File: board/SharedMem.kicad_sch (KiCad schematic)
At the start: 10 parts, among them U19 HM628512LP-5, U20 HM628512LP-5, U21 HM628512LP-5, U22 HM628512LP-5, U23 74F139

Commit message: Board V1.1G
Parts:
- U19, U20, U21, U22: footprint Package_DIP:DIP-32_W15.24mm_Socket_LongPads -> Package_SO:SOP-32_11.305x20.495mm_P1.27mm
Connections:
- net A0 renamed A_MEM0
- net A1 renamed A_MEM1
- net A10 renamed A_MEM10
- net A11 renamed A_MEM11
- net A12 renamed A_MEM12
- net A2 renamed A_MEM2
- net A3 renamed A_MEM3
- net A4 renamed A_MEM4
- net A5 renamed A_MEM5
- net A6 renamed A_MEM6
- net A7 renamed A_MEM7
- net A8 renamed A_MEM8
- net A9 renamed A_MEM9
- net D0 renamed D_MEM0
- net D1 renamed D_MEM1
- net D2 renamed D_MEM2
- net D3 renamed D_MEM3
- net D4 renamed D_MEM4
- net D5 renamed D_MEM5
- net D6 renamed D_MEM6
- net D7 renamed D_MEM7

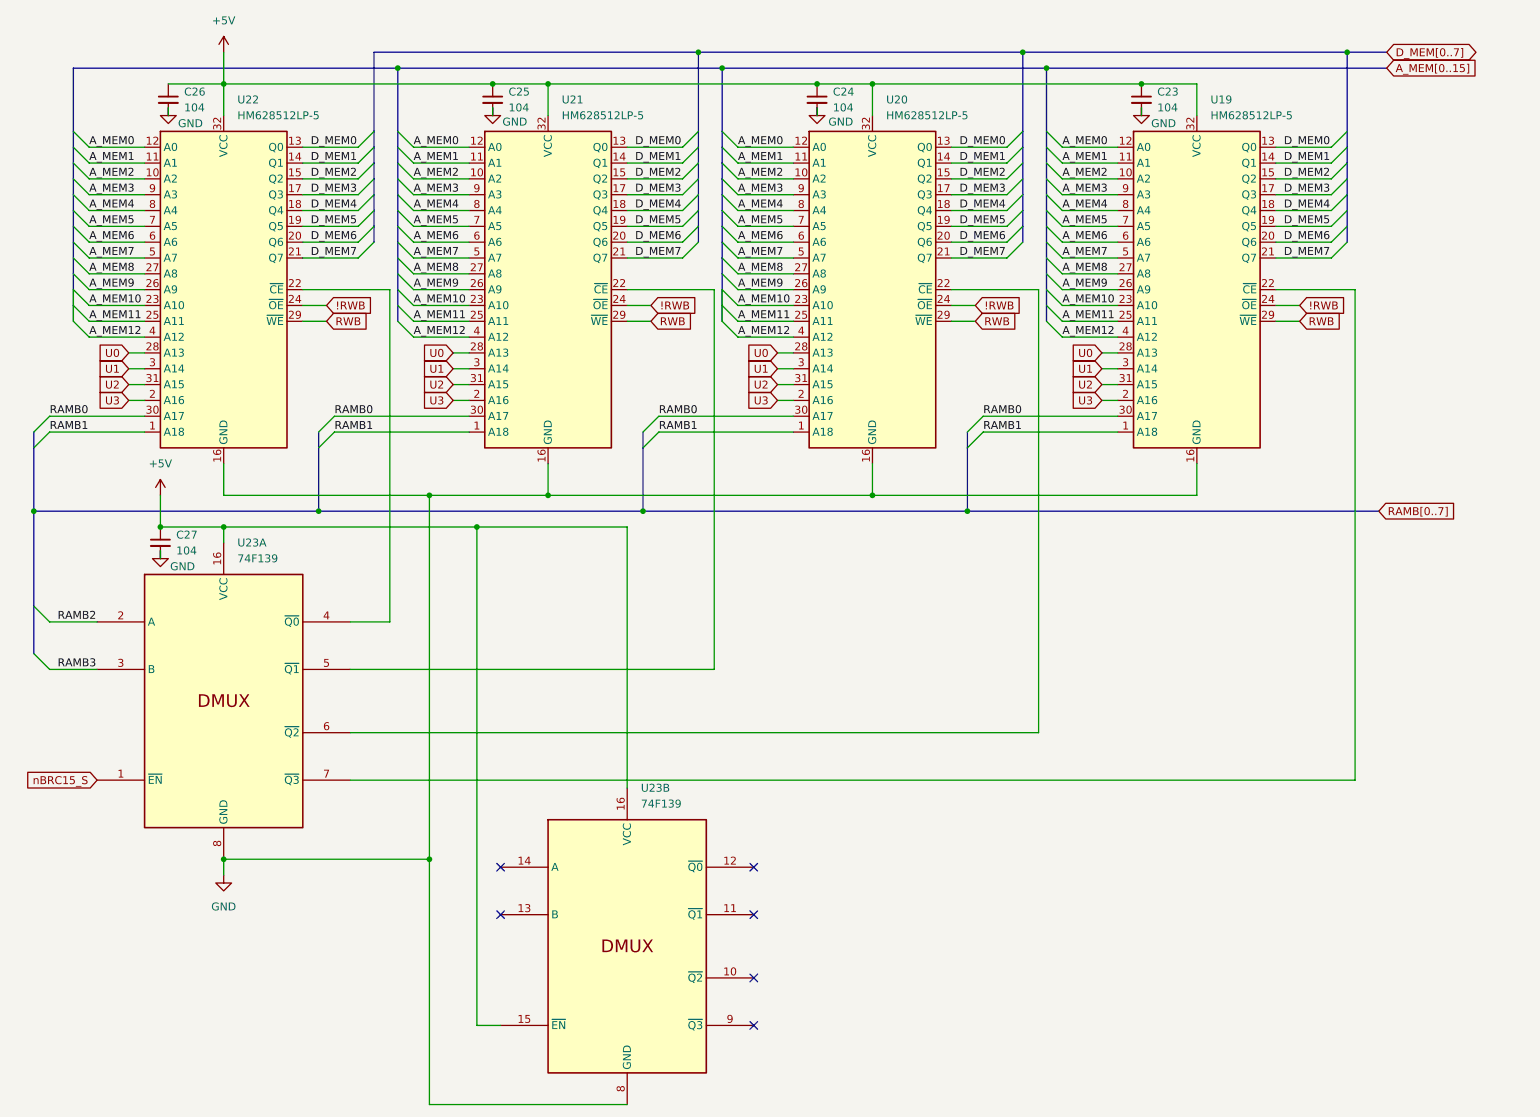
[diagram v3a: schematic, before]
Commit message: V1.3C without board traces
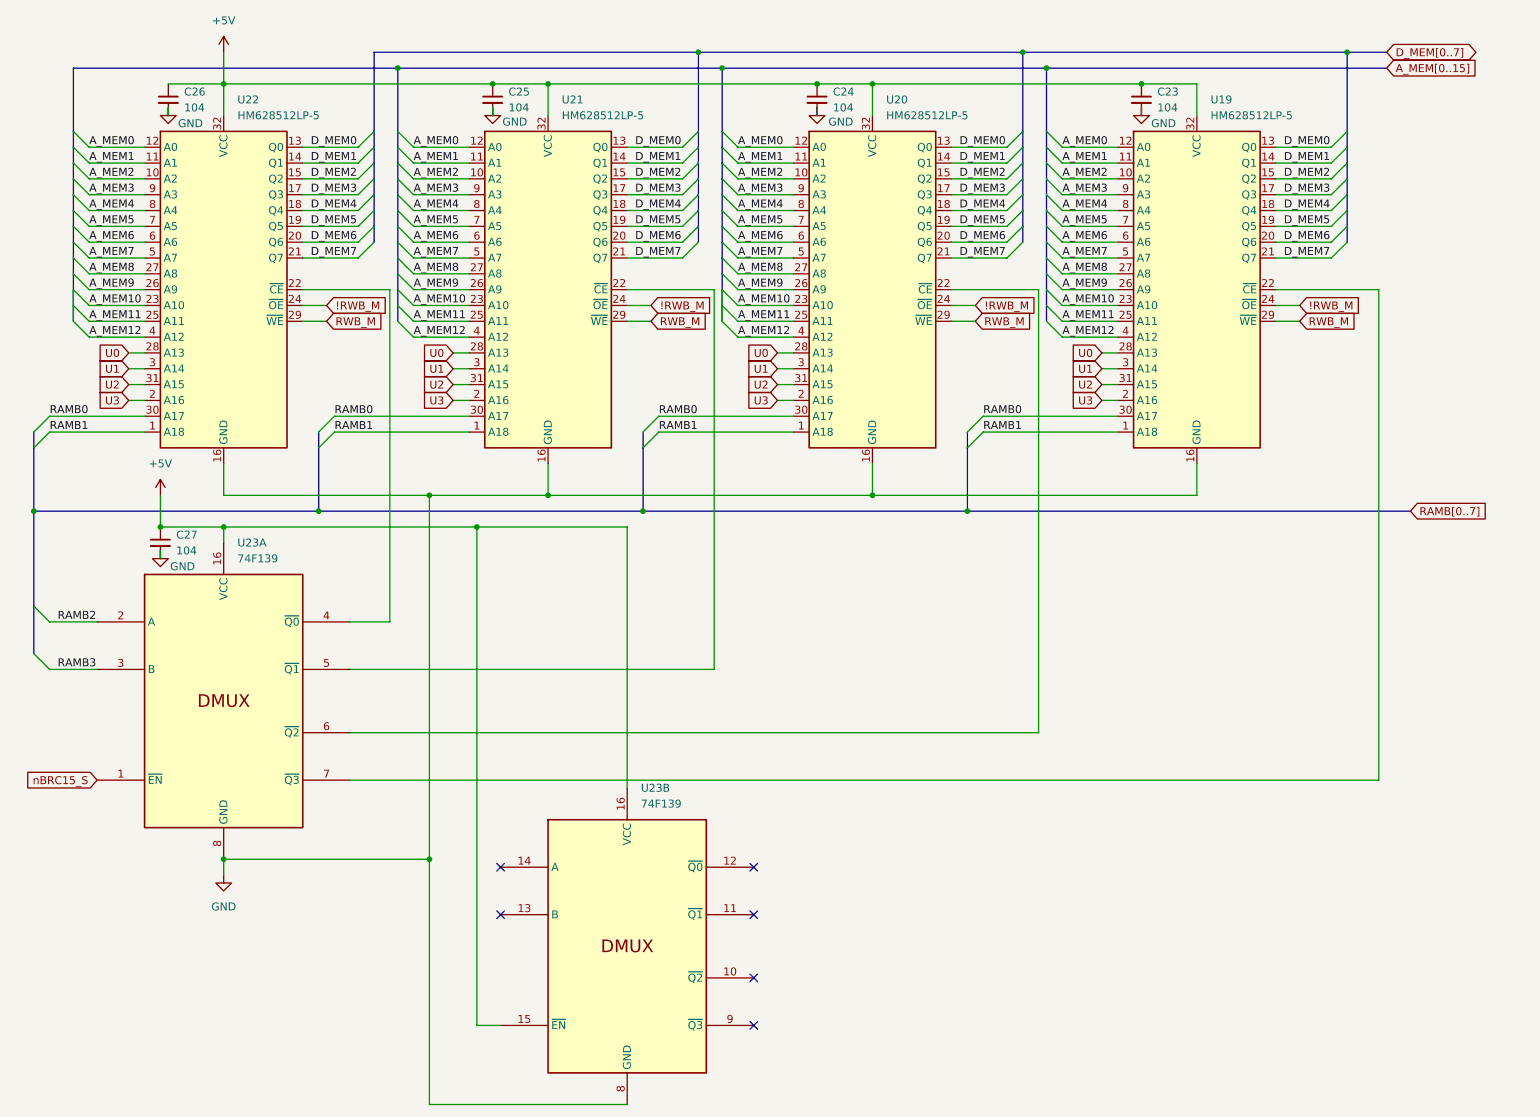
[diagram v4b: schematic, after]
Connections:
- net !RWB renamed !RWB_M
- net RWB renamed RWB_M
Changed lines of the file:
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@@
 	(title_block
 		(title "Shared RAM Banks")
-		(date "2025-04-15")
-		(rev "1.3")
+		(date "2025-04-23")
+		(rev "1.3C")
 		(company "Data Tuning")
 		(comment 1 "Hydra 16")
@@
 	(wire
 		(pts
-			(xy 232.41 148.59) (xy 232.41 69.85)
+			(xy 236.22 148.59) (xy 236.22 69.85)
 		)
 		(stroke
@@
 	(wire
 		(pts
-			(xy 71.12 148.59) (xy 232.41 148.59)
+			(xy 71.12 148.59) (xy 236.22 148.59)
 		)
 		(stroke
@@
 	(wire
 		(pts
-			(xy 219.71 69.85) (xy 232.41 69.85)
+			(xy 219.71 69.85) (xy 236.22 69.85)
 		)
 		(stroke
@@
 	(bus
 		(pts
-			(xy 170.18 105.41) (xy 236.22 105.41)
+			(xy 170.18 105.41) (xy 241.3 105.41)
 		)
 		(stroke
@@
 	(global_label "RAMB[0..7]"
 		(shape input)
-		(at 236.22 105.41 0)
+		(at 241.3 105.41 0)
 		(fields_autoplaced yes)
 		(effects
@@
 		)
 		(property "Intersheetrefs" "${INTERSHEET_REFS}"
-			(at 249.6072 105.41 0)
+			(at 254.6872 105.41 0)
 			(effects
 				(font
@@
 		)
 	)
-	(global_label "RWB"
+	(global_label "RWB_M"
 		(shape input)
 		(at 119.38 74.93 0)
@@
 		)
 		(property "Intersheetrefs" "${INTERSHEET_REFS}"
-			(at 112.4034 74.93 0)
+			(at 128.7756 74.93 0)
 			(effects
 				(font
 					(size 1.27 1.27)
 				)
-				(justify right)
+				(justify left)
 				(hide yes)
 			)
@@
 		)
 	)
-	(global_label "!RWB"
+	(global_label "!RWB_M"
 		(shape input)
 		(at 119.38 72.39 0)
@@
 		)
 		(property "Intersheetrefs" "${INTERSHEET_REFS}"
-			(at 126.9614 72.39 0)
+			(at 129.3804 72.39 0)
 			(effects
 				(font
@@
 		)
 	)
-	(global_label "!RWB"
+	(global_label "!RWB_M"
 		(shape input)
 		(at 223.52 72.39 0)
@@
 		)
 		(property "Intersheetrefs" "${INTERSHEET_REFS}"
-			(at 231.1014 72.39 0)
+			(at 233.5204 72.39 0)
 			(effects
 				(font
@@
 		)
 	)
-	(global_label "RWB"
+	(global_label "RWB_M"
 		(shape input)
 		(at 171.45 74.93 0)
@@
 		)
 		(property "Intersheetrefs" "${INTERSHEET_REFS}"
-			(at 164.4734 74.93 0)
+			(at 180.8456 74.93 0)
 			(effects
 				(font
 					(size 1.27 1.27)
 				)
-				(justify right)
+				(justify left)
 				(hide yes)
 			)
@@
 		)
 	)
-	(global_label "!RWB"
+	(global_label "!RWB_M"
 		(shape input)
 		(at 171.45 72.39 0)
@@
 		)
 		(property "Intersheetrefs" "${INTERSHEET_REFS}"
-			(at 179.0314 72.39 0)
+			(at 181.4504 72.39 0)
 			(effects
 				(font
@@
 		)
 	)
-	(global_label "!RWB"
+	(global_label "!RWB_M"
 		(shape input)
 		(at 67.31 72.39 0)
@@
 		)
 		(property "Intersheetrefs" "${INTERSHEET_REFS}"
-			(at 74.8914 72.39 0)
+			(at 77.3104 72.39 0)
 			(effects
 				(font
@@
 		)
 	)
-	(global_label "RWB"
+	(global_label "RWB_M"
 		(shape input)
 		(at 67.31 74.93 0)
@@
 		)
 		(property "Intersheetrefs" "${INTERSHEET_REFS}"
-			(at 60.3334 74.93 0)
+			(at 76.7056 74.93 0)
 			(effects
 				(font
 					(size 1.27 1.27)
 				)
-				(justify right)
+				(justify left)
 				(hide yes)
 			)
 		)
 	)
-	(global_label "RWB"
+	(global_label "RWB_M"
 		(shape input)
 		(at 223.52 74.93 0)
@@
 		)
 		(property "Intersheetrefs" "${INTERSHEET_REFS}"
-			(at 216.5434 74.93 0)
+			(at 232.9156 74.93 0)
 			(effects
 				(font
 					(size 1.27 1.27)
 				)
-				(justify right)
+				(justify left)
 				(hide yes)
 			)

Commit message: V1.4E
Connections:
- net A_MEM0 renamed A0
- net A_MEM1 renamed A1
- net A_MEM10 renamed A10
- net A_MEM11 renamed A11
- net A_MEM12 renamed A12
- net A_MEM2 renamed A2
- net A_MEM3 renamed A3
- net A_MEM4 renamed A4
- net A_MEM5 renamed A5
- net A_MEM6 renamed A6
- net A_MEM7 renamed A7
- net A_MEM8 renamed A8
- net A_MEM9 renamed A9
- net D_MEM0 renamed D0
- net D_MEM1 renamed D1
- net D_MEM2 renamed D2
- net D_MEM3 renamed D3
- net D_MEM4 renamed D4
- net D_MEM5 renamed D5
- net D_MEM6 renamed D6
- net D_MEM7 renamed D7

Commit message: Version 1.7A: More rearrangement, partial wiring of PDB, addition of W register
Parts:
- renumbered C27 to C33, C26 to C34, C25 to C35, C24 to C36, C23 to C37, U22 to U25, U23 to U26, U21 to U27, U20 to U28, U19 to U29
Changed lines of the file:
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@@
 	(title_block
 		(title "Shared RAM Banks")
-		(date "2025-04-23")
-		(rev "1.3C")
+		(date "2025-09-18")
+		(rev "1.6F")
 		(company "Data Tuning")
 		(comment 1 "Hydra 16")
@@
 		(dnp no)
 		(fields_autoplaced yes)
-		(property "Reference" "U20"
+		(property "Reference" "U28"
 			(at 157.1341 39.37 0)
 			(effects
@@
 			(project "hydra-16"
 				(path "/ef29fc71-3fec-48b5-8a1a-46bee537a98c/0b66303c-ed46-41df-a285-d041c923c3ce"
-					(reference "U20")
+					(reference "U28")
 					(unit 1)
 				)
@@
 		(dnp no)
 		(fields_autoplaced yes)
-		(property "Reference" "C26"
+		(property "Reference" "C34"
 			(at 44.45 38.1062 0)
 			(effects
@@
 			(project "6502_x256"
 				(path "/ef29fc71-3fec-48b5-8a1a-46bee537a98c/0b66303c-ed46-41df-a285-d041c923c3ce"
-					(reference "C26")
+					(reference "C34")
 					(unit 1)
 				)
@@
 		(dnp no)
 		(fields_autoplaced yes)
-		(property "Reference" "C24"
+		(property "Reference" "C36"
 			(at 148.59 38.1062 0)
 			(effects
@@
 			(project "6502_x256"
 				(path "/ef29fc71-3fec-48b5-8a1a-46bee537a98c/0b66303c-ed46-41df-a285-d041c923c3ce"
-					(reference "C24")
+					(reference "C36")
 					(unit 1)
 				)
@@
 		(on_board yes)
 		(dnp no)
-		(property "Reference" "#PWR028"
+		(property "Reference" "#PWR017"
 			(at 93.98 46.99 0)
 			(effects
@@
 			(project "6502_x256"
 				(path "/ef29fc71-3fec-48b5-8a1a-46bee537a98c/0b66303c-ed46-41df-a285-d041c923c3ce"
-					(reference "#PWR028")
+					(reference "#PWR017")
 					(unit 1)
 				)
@@
 		(dnp no)
 		(fields_autoplaced yes)
-		(property "Reference" "#PWR041"
+		(property "Reference" "#PWR012"
 			(at 40.64 106.68 0)
 			(effects
@@
 			(project "hydra-16"
 				(path "/ef29fc71-3fec-48b5-8a1a-46bee537a98c/0b66303c-ed46-41df-a285-d041c923c3ce"
-					(reference "#PWR041")
+					(reference "#PWR012")
 					(unit 1)
 				)
@@
 		(on_board yes)
 		(dnp no)
-		(property "Reference" "#PWR029"
+		(property "Reference" "#PWR014"
 			(at 41.91 46.99 0)
 			(effects
@@
 			(project "6502_x256"
 				(path "/ef29fc71-3fec-48b5-8a1a-46bee537a98c/0b66303c-ed46-41df-a285-d041c923c3ce"
-					(reference "#PWR029")
+					(reference "#PWR014")
 					(unit 1)
 				)
@@
 		(dnp no)
 		(fields_autoplaced yes)
-		(property "Reference" "C27"
+		(property "Reference" "C33"
 			(at 43.18 109.2262 0)
 			(effects
@@
 			(project "6502_x256"
 				(path "/ef29fc71-3fec-48b5-8a1a-46bee537a98c/0b66303c-ed46-41df-a285-d041c923c3ce"
-					(reference "C27")
+					(reference "C33")
 					(unit 1)
 				)
@@
 		(dnp no)
 		(fields_autoplaced yes)
-		(property "Reference" "U19"
+		(property "Reference" "U29"
 			(at 209.2041 39.37 0)
 			(effects
@@
 			(project "hydra-16"
 				(path "/ef29fc71-3fec-48b5-8a1a-46bee537a98c/0b66303c-ed46-41df-a285-d041c923c3ce"
-					(reference "U19")
+					(reference "U29")
 					(unit 1)
 				)
@@
 		(on_board yes)
 		(dnp no)
-		(property "Reference" "#PWR026"
+		(property "Reference" "#PWR019"
 			(at 198.12 46.99 0)
 			(effects
@@
 			(project "6502_x256"
 				(path "/ef29fc71-3fec-48b5-8a1a-46bee537a98c/0b66303c-ed46-41df-a285-d041c923c3ce"
-					(reference "#PWR026")
+					(reference "#PWR019")
 					(unit 1)
 				)
@@
 		(dnp no)
 		(fields_autoplaced yes)
-		(property "Reference" "C25"
+		(property "Reference" "C35"
 			(at 96.52 38.1062 0)
 			(effects
@@
 			(project "6502_x256"
 				(path "/ef29fc71-3fec-48b5-8a1a-46bee537a98c/0b66303c-ed46-41df-a285-d041c923c3ce"
-					(reference "C25")
+					(reference "C35")
 					(unit 1)
 				)
@@
 		(dnp no)
 		(fields_autoplaced yes)
-		(property "Reference" "U23"
+		(property "Reference" "U26"
 			(at 117.7641 149.86 0)
 			(effects
@@
 			(project "hydra-16"
 				(path "/ef29fc71-3fec-48b5-8a1a-46bee537a98c/0b66303c-ed46-41df-a285-d041c923c3ce"
-					(reference "U23")
+					(reference "U26")
 					(unit 2)
 				)
@@
 		(on_board yes)
 		(dnp no)
-		(property "Reference" "#PWR027"
+		(property "Reference" "#PWR018"
 			(at 146.05 46.99 0)
 			(effects
@@
 			(project "6502_x256"
 				(path "/ef29fc71-3fec-48b5-8a1a-46bee537a98c/0b66303c-ed46-41df-a285-d041c923c3ce"
-					(reference "#PWR027")
+					(reference "#PWR018")
 					(unit 1)
 				)
@@
 		(dnp no)
 		(fields_autoplaced yes)
-		(property "Reference" "U22"
+		(property "Reference" "U25"
 			(at 52.9941 39.37 0)
 			(effects
@@
 			(project "hydra-16"
 				(path "/ef29fc71-3fec-48b5-8a1a-46bee537a98c/0b66303c-ed46-41df-a285-d041c923c3ce"
-					(reference "U22")
+					(reference "U25")
 					(unit 1)
 				)
@@
 		(dnp no)
 		(fields_autoplaced yes)
-		(property "Reference" "C23"
+		(property "Reference" "C37"
 			(at 200.66 38.1062 0)
 			(effects
@@
 			(project "6502_x256"
 				(path "/ef29fc71-3fec-48b5-8a1a-46bee537a98c/0b66303c-ed46-41df-a285-d041c923c3ce"
-					(reference "C23")
+					(reference "C37")
 					(unit 1)
 				)
@@
 		(dnp no)
 		(fields_autoplaced yes)
-		(property "Reference" "#PWR06"
+		(property "Reference" "#PWR016"
 			(at 50.8 170.18 0)
 			(effects
@@
 			(project ""
 				(path "/ef29fc71-3fec-48b5-8a1a-46bee537a98c/0b66303c-ed46-41df-a285-d041c923c3ce"
-					(reference "#PWR06")
+					(reference "#PWR016")
 					(unit 1)
 				)
@@
 		(dnp no)
 		(fields_autoplaced yes)
-		(property "Reference" "#PWR05"
+		(property "Reference" "#PWR015"
 			(at 50.8 35.56 0)
 			(effects
@@
 			(project ""
 				(path "/ef29fc71-3fec-48b5-8a1a-46bee537a98c/0b66303c-ed46-41df-a285-d041c923c3ce"
-					(reference "#PWR05")
+					(reference "#PWR015")
 					(unit 1)
 				)
@@
 		(dnp no)
 		(fields_autoplaced yes)
-		(property "Reference" "U21"
+		(property "Reference" "U27"
 			(at 105.0641 39.37 0)
 			(effects
@@
 			(project "6502_x256"
 				(path "/ef29fc71-3fec-48b5-8a1a-46bee537a98c/0b66303c-ed46-41df-a285-d041c923c3ce"
-					(reference "U21")
+					(reference "U27")
 					(unit 1)
 				)
@@
 		(dnp no)
 		(fields_autoplaced yes)
-		(property "Reference" "U23"
+		(property "Reference" "U26"
 			(at 52.9941 110.49 0)
 			(effects
@@
 			(project ""
 				(path "/ef29fc71-3fec-48b5-8a1a-46bee537a98c/0b66303c-ed46-41df-a285-d041c923c3ce"
-					(reference "U23")
+					(reference "U26")
 					(unit 1)
 				)
@@
 		(on_board yes)
 		(dnp no)
-		(property "Reference" "#PWR030"
+		(property "Reference" "#PWR013"
 			(at 40.64 118.11 0)
 			(effects
@@
 			(project "6502_x256"
 				(path "/ef29fc71-3fec-48b5-8a1a-46bee537a98c/0b66303c-ed46-41df-a285-d041c923c3ce"
-					(reference "#PWR030")
+					(reference "#PWR013")
 					(unit 1)
 				)

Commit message: Version 1.7A: Partial wireup
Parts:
- removed unit 2 of U26
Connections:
- no-connect marks 6 -> 0
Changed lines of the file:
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@@
 		(title "Shared RAM Banks")
 		(date "2025-09-18")
-		(rev "1.6F")
+		(rev "1.7A")
 		(company "Data Tuning")
 		(comment 1 "Hydra 16")
@@
 	)
 	(junction
-		(at 91.44 107.95)
-		(diameter 0)
-		(color 0 0 0 0)
-	)
-	(junction
 		(at 130.81 34.29)
 		(diameter 0)
@@
 	)
 	(junction
-		(at 83.82 161.29)
-		(diameter 0)
-		(color 0 0 0 0)
-	)
-	(junction
 		(at 146.05 36.83)
 		(diameter 0)
@@
 		(color 0 0 0 0)
 	)
-	(no_connect
-		(at 135.89 162.56)
-	)
-	(no_connect
-		(at 135.89 180.34)
-	)
-	(no_connect
-		(at 135.89 187.96)
-	)
-	(no_connect
-		(at 95.25 170.18)
-	)
-	(no_connect
-		(at 95.25 162.56)
-	)
-	(no_connect
-		(at 135.89 170.18)
-	)
 	(bus_entry
 		(at 78.74 74.93)
@@
 	(wire
 		(pts
-			(xy 91.44 107.95) (xy 50.8 107.95)
-		)
-		(stroke
-			(width 0)
-			(type default)
-		)
-	)
-	(wire
-		(pts
 			(xy 191.77 85.09) (xy 194.31 85.09)
 		)
@@
 	(wire
 		(pts
-			(xy 83.82 200.66) (xy 115.57 200.66)
-		)
-		(stroke
-			(width 0)
-			(type default)
-		)
-	)
-	(wire
-		(pts
-			(xy 115.57 149.86) (xy 115.57 107.95)
-		)
-		(stroke
-			(width 0)
-			(type default)
-		)
-	)
-	(wire
-		(pts
 			(xy 154.94 36.83) (xy 146.05 36.83)
 		)
@@
 		)
 	)
-	(wire
-		(pts
-			(xy 83.82 161.29) (xy 83.82 200.66)
-		)
-		(stroke
-			(width 0)
-			(type default)
-		)
-	)
 	(bus
 		(pts
@@
 	(wire
 		(pts
-			(xy 115.57 107.95) (xy 91.44 107.95)
+			(xy 50.8 107.95) (xy 115.57 107.95)
 		)
 		(stroke
@@
 		)
 	)
-	(wire
-		(pts
-			(xy 95.25 187.96) (xy 91.44 187.96)
-		)
-		(stroke
-			(width 0)
-			(type default)
-		)
-	)
 	(bus
 		(pts
@@
 	(wire
 		(pts
-			(xy 91.44 187.96) (xy 91.44 107.95)
-		)
-		(stroke
-			(width 0)
-			(type default)
-		)
-	)
-	(wire
-		(pts
 			(xy 22.86 130.81) (xy 30.48 130.81)
 		)
@@
 				)
 			)
-		)
-	)
-	(symbol
-		(lib_id "74xx_IEEE:74LS139")
-		(at 115.57 175.26 0)
-		(unit 2)
-		(exclude_from_sim no)
-		(in_bom yes)
-		(on_board yes)
-		(dnp no)
-		(fields_autoplaced yes)
-		(property "Reference" "U26"
-			(at 117.7641 149.86 0)
-			(effects
-				(font
-					(size 1.27 1.27)
-				)
-				(justify left)
-			)
-		)
-		(property "Value" "74F139"
-			(at 117.7641 152.4 0)
-			(effects
-				(font
-					(size 1.27 1.27)
-				)
-				(justify left)
-			)
-		)
-		(property "Footprint" "Package_DIP:DIP-16_W7.62mm_Socket_LongPads"
-			(at 115.57 175.26 0)
-			(effects
-				(font
-					(size 1.27 1.27)
-				)
-				(hide yes)
-			)
-		)
-		(property "Datasheet" "http://www.ti.com/lit/ds/symlink/sn74ls139a.pdf"
-			(at 115.57 175.26 0)
-			(effects
-				(font
-					(size 1.27 1.27)
-				)
-				(hide yes)
-			)
-		)
-		(property "Description" "Dual Decoder 1 of 4, Active low outputs"
-			(at 115.57 175.26 0)
-			(effects
-				(font
-					(size 1.27 1.27)
-				)
-				(hide yes)
-			)
-		)
-		(pin "1"
-		)
-		(pin "2"
-		)
-		(pin "5"
-		)
-		(pin "16"
-		)
-		(pin "13"
-		)
-		(pin "3"
-		)
-		(pin "4"
-		)
-		(pin "10"
-		)
-		(pin "11"
-		)
-		(pin "8"
-		)
-		(pin "6"
-		)
-		(pin "12"
-		)
-		(pin "14"
-		)
-		(pin "15"
-		)
-		(pin "7"
-		)
-		(pin "9"
-		)
-		(instances
-			(project "hydra-16"
-				(path "/ef29fc71-3fec-48b5-8a1a-46bee537a98c/0b66303c-ed46-41df-a285-d041c923c3ce"
-					(reference "U26")
-					(unit 2)
-				)
-			)
